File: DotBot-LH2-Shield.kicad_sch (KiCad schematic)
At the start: 15 parts, among them J1 Conn_01x04, J1 Conn_01x10, U1 LSM303AGR, U4 TS4231

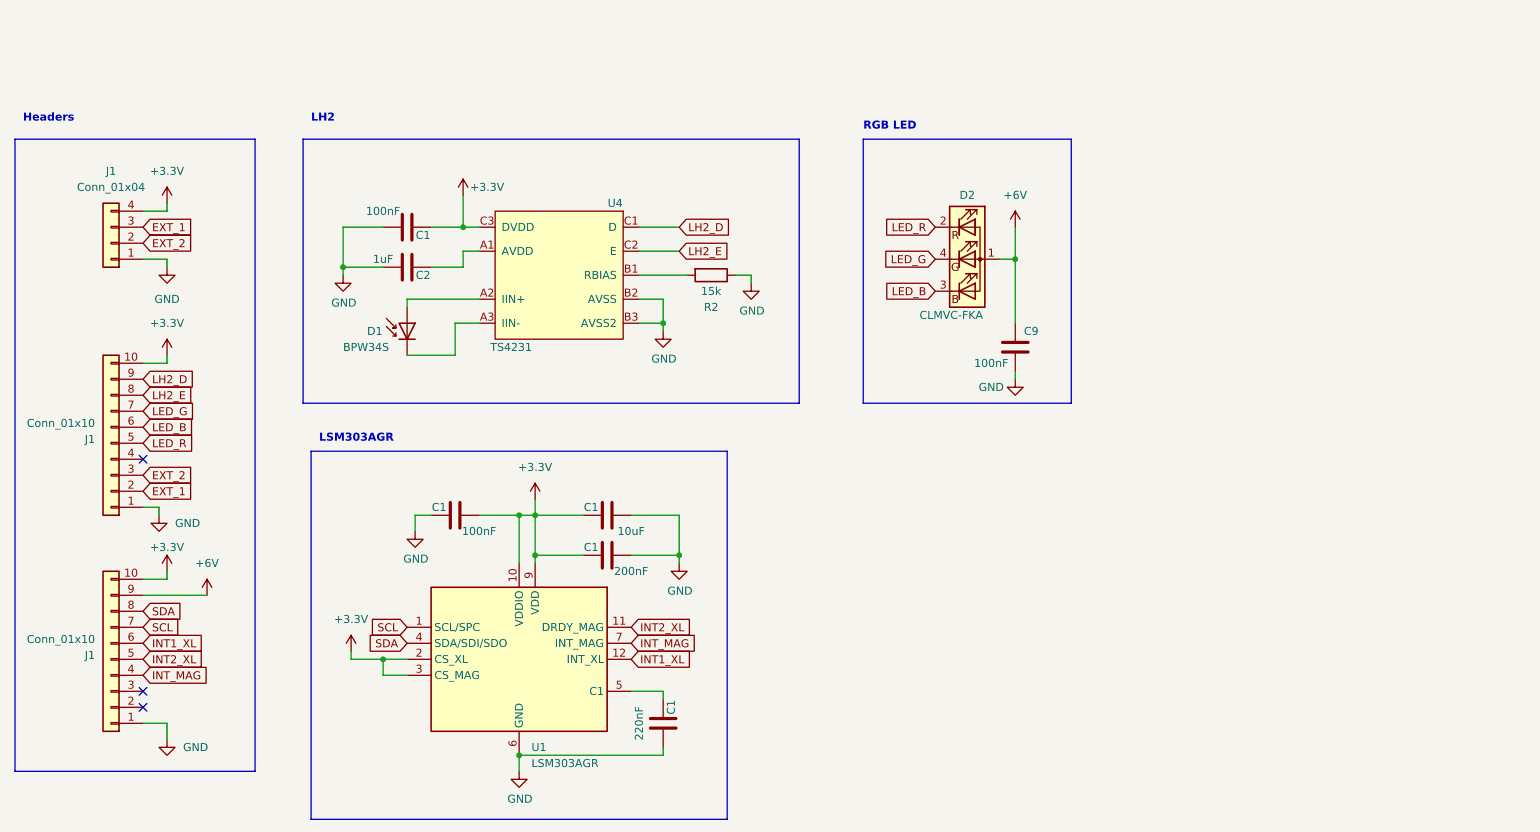
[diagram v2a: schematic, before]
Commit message: DotBot-LH2-Shield: rework IMU and RGB LED
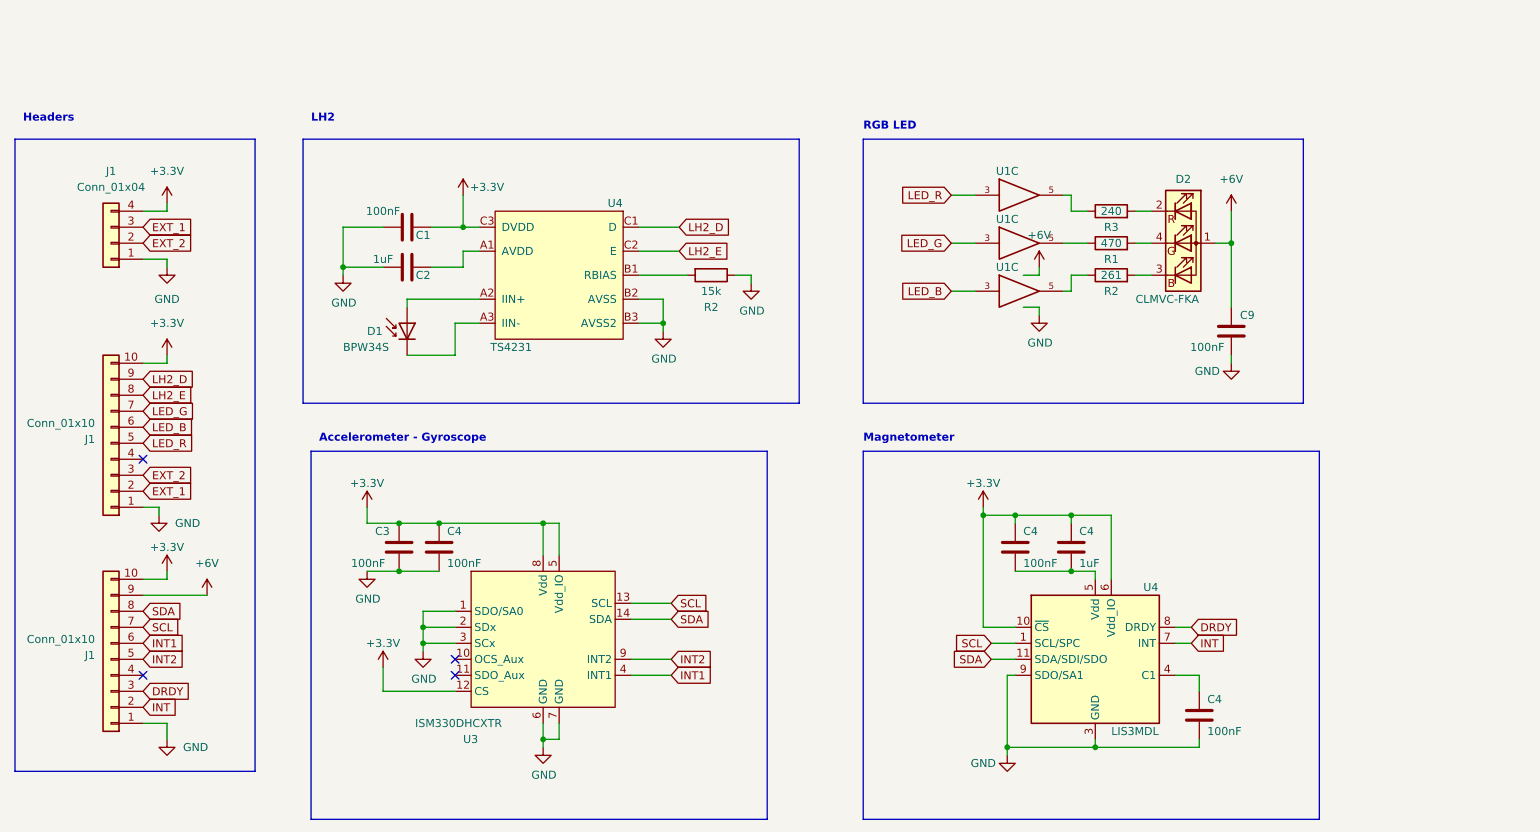
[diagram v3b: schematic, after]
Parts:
- removed C1: 200nF, Capacitor_SMD:C_0603_1608Metric, symbol Device:C
- removed C1: 220nF, Capacitor_SMD:C_0603_1608Metric, symbol Device:C
- removed C1: 100nF, Capacitor_SMD:C_0603_1608Metric, symbol Device:C
- removed C1: 10uF, Capacitor_SMD:C_0603_1608Metric, symbol Device:C
- removed U1: LSM303AGR, Package_LGA:LGA-12_2x2mm_P0.5mm, symbol Sensor_Motion:LSM303C
- added C3, C4 (x3): 100nF, Capacitor_SMD:C_0603_1608Metric, symbol Device:C
- added C4: 1uF, Capacitor_SMD:C_0603_1608Metric, symbol Device:C
- added R1: 470, Resistor_SMD:R_0603_1608Metric, symbol Device:R
- added R2: 261, Resistor_SMD:R_0603_1608Metric, symbol Device:R
- added R3: 240, Resistor_SMD:R_0603_1608Metric, symbol Device:R
- added U1 (x3): 74LVC3G34, DotBot:SOT833-1-8_1x1.95_Pitch0.5mm, symbol 74xGxx:74LVC3G34
- added U3: ISM330DHCXTR, Package_LGA:Bosch_LGA-14_3x2.5mm_P0.5mm, symbol DotBot:ISM330DHCXTR
- added U4: LIS3MDL, Package_LGA:LGA-12_2x2mm_P0.5mm, symbol Sensor_Magnetic:LIS3MDL
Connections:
- net +3V3: now also C3.1, C4.1, C4.1, C4.1, U3.12 (CS), U3.5 (Vdd_IO), U3.8 (Vdd), U4.10 (~{CS}), U4.6 (Vdd_IO)
- net +6V: now also U1.8 (VCC), U1.8 (VCC), U1.8 (VCC)
- net GND: now also C3.2, C4.2, C4.2, U1.4 (GND), U1.4 (GND), U1.4 (GND), U3.1 (SDO/SA0), U3.2 (SDx), U3.3 (SCx), U3.6 (GND), U3.7 (GND), U4.12 (GND), U4.2 (GND), U4.3 (GND), U4.9 (SDO/SA1)
- net LED_B: now also U1.3; no longer D2.3 (BK)
- net LED_G: now also U1.3; no longer D2.4 (GK)
- net LED_R: now also U1.3; no longer D2.2 (RK)
- net SCL: now also U3.13 (SCL), U4.1 (SCL/SPC)
- net SDA: now also U3.14 (SDA), U4.11 (SDA/SDI/SDO)
- net INT: now reaches J1.2 (Pin_2)
- net INT: now also U4.7 (INT)
- net DRDY: now reaches J1.3 (Pin_3)
- net DRDY: now also U4.8 (DRDY)
- net INT1_XL renamed INT1
- net INT1: now also U3.4 (INT1)
- net INT2_XL renamed INT2
- net INT2: now also U3.9 (INT2)
- net INT_MAG: no longer names the net of J1.4 (Pin_4)
- new net: C4.2, C4.2, U4.5 (Vdd)
- new net: D2.2 (RK), R3.2
- new net: D2.3 (BK), R2.2
- new net: D2.4 (GK), R1.2
- new net: R1.1, U1.5
- new net: R2.1, U1.5
- new net: C4.1, U4.4 (C1)
- new net: R3.1, U1.5
- no-connect marks 3 -> 4
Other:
- note added: "Accelerometer - Gyroscope"
- note added: "Magnetometer"
- note removed: "LSM303AGR"
- moved on the sheet: C9, D2

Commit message: DotBot-LH2-Shield: update BOM
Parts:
- C3, C4: Price $0.1 -> 0.1
- R1: Price $0.35 -> 0.35
- R2, R3: Price $0.19 -> 0.19
- U1: Price $0.46 -> 0.46
- U3: Price $11.34 -> 11.34
- U4: Link (none) -> https://www.digikey.fr/short/rzjc85mw; Manufacturer (none) -> STMicroelectronics; Mfr Part Number (none) -> 497-13892-1-ND; Price (none) -> 1.962
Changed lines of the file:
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@@
       (effects (font (size 1.27 1.27)) hide)
     )
-    (property "Price" "$0.1" (at 195.58 99.06 0)
+    (property "Price" "0.1" (at 195.58 99.06 0)
       (effects (font (size 1.27 1.27)) hide)
     )
@@
       (effects (font (size 1.27 1.27)) hide)
     )
-    (property "Datasheet" "~" (at 213.36 52.07 0)
+    (property "Datasheet" "https://media.digikey.com/pdf/Data%20Sheets/CREE%20Power/CLMVC-FKA_Rev13_2021.pdf" (at 213.36 52.07 0)
       (effects (font (size 1.27 1.27)) hide)
     )
@@
       (effects (font (size 1.27 1.27)) hide)
     )
-    (property "Price" "$0.1" (at 88.9 99.06 0)
+    (property "Price" "0.1" (at 88.9 99.06 0)
       (effects (font (size 1.27 1.27)) hide)
     )
@@
       (effects (font (size 1.27 1.27)) hide)
     )
-    (property "Price" "$0.46" (at 187.96 50.8 0)
+    (property "Price" "0.46" (at 187.96 50.8 0)
       (effects (font (size 1.27 1.27)) hide)
     )
@@
       (effects (font (size 1.27 1.27)) hide)
     )
-    (property "Price" "$0.46" (at 187.96 58.42 0)
+    (property "Price" "0.46" (at 187.96 58.42 0)
       (effects (font (size 1.27 1.27)) hide)
     )
@@
       (effects (font (size 1.27 1.27)) hide)
     )
-    (property "Price" "$0.1" (at 95.25 99.06 0)
+    (property "Price" "0.1" (at 95.25 99.06 0)
       (effects (font (size 1.27 1.27)) hide)
     )
@@
       (effects (font (size 1.27 1.27)) hide)
     )
-    (property "Price" "$0.1" (at 186.69 99.06 0)
+    (property "Price" "0.1" (at 186.69 99.06 0)
       (effects (font (size 1.27 1.27)) hide)
     )
@@
       (effects (font (size 1.27 1.27)) hide)
     )
-    (property "Price" "$0.19" (at 201.93 55.88 0)
+    (property "Price" "0.19" (at 201.93 55.88 0)
       (effects (font (size 1.27 1.27)) hide)
     )
@@
     )
     (property "Datasheet" "https://www.st.com/resource/en/datasheet/lis3mdl.pdf" (at 237.49 127 0)
+      (effects (font (size 1.27 1.27)) hide)
+    )
+    (property "Link" "https://www.digikey.fr/short/rzjc85mw" (at 199.39 116.84 0)
+      (effects (font (size 1.27 1.27)) hide)
+    )
+    (property "Manufacturer" "STMicroelectronics" (at 199.39 116.84 0)
+      (effects (font (size 1.27 1.27)) hide)
+    )
+    (property "Mfr Part Number" "497-13892-1-ND" (at 199.39 116.84 0)
+      (effects (font (size 1.27 1.27)) hide)
+    )
+    (property "Price" "1.962" (at 199.39 116.84 0)
       (effects (font (size 1.27 1.27)) hide)
     )
@@
       (effects (font (size 1.27 1.27)) hide)
     )
-    (property "Price" "$0.1" (at 215.9 125.73 0)
+    (property "Price" "0.1" (at 215.9 125.73 0)
       (effects (font (size 1.27 1.27)) hide)
     )
@@
       (effects (font (size 1.27 1.27)) hide)
     )
-    (property "Price" "$0.35" (at 201.93 50.8 0)
+    (property "Price" "0.35" (at 201.93 50.8 0)
       (effects (font (size 1.27 1.27)) hide)
     )
@@
       (effects (font (size 1.27 1.27)) hide)
     )
-    (property "Price" "$0.19" (at 201.93 45.72 0)
+    (property "Price" "0.19" (at 201.93 45.72 0)
       (effects (font (size 1.27 1.27)) hide)
     )
@@
       (effects (font (size 1.27 1.27)) hide)
     )
-    (property "Price" "$0.46" (at 187.96 43.18 0)
+    (property "Price" "0.46" (at 187.96 43.18 0)
       (effects (font (size 1.27 1.27)) hide)
     )
@@
       (effects (font (size 1.27 1.27)) hide)
     )
-    (property "Price" "$11.34" (at 110.49 113.03 0)
-      (effects (font (size 1.27 1.27)) hide)
-    )
+    (property "Price" "11.34" (at 110.49 113.03 0)
+      (effects (font (size 1.27 1.27)) hide)
+    )

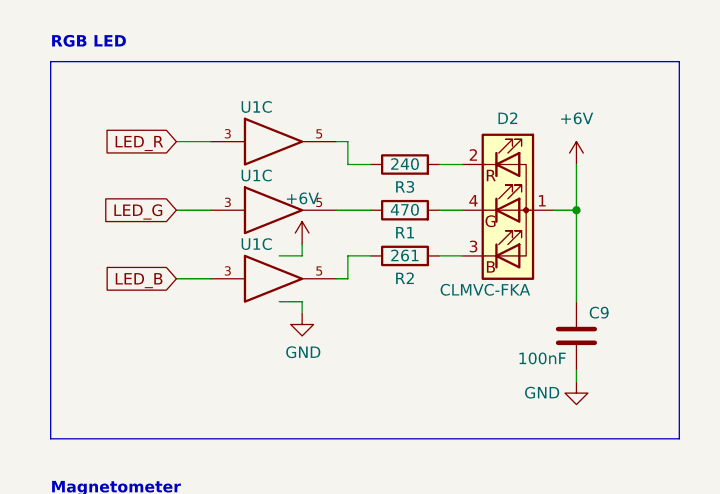
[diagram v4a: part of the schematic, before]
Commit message: Recalculate RGB resistors for 6v instead of 3.7v
the resistors for the RGB led were calculated for the minimote, which works with a  Li-ion 3.7v battery
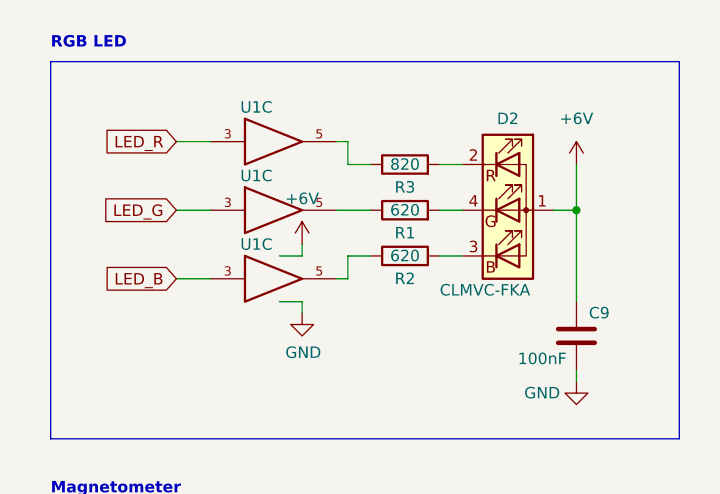
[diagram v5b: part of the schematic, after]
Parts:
- R1: value 470 -> 620
- R2: value 261 -> 620
- R3: value 240 -> 820
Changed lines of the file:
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@@
       (effects (font (size 1.27 1.27)))
     )
-    (property "Value" "261" (at 201.93 55.88 90)
+    (property "Value" "620" (at 201.93 55.88 90)
       (effects (font (size 1.27 1.27)))
     )
@@
       (effects (font (size 1.27 1.27)))
     )
-    (property "Value" "470" (at 201.93 50.8 90)
+    (property "Value" "620" (at 201.93 50.8 90)
       (effects (font (size 1.27 1.27)))
     )
@@
       (effects (font (size 1.27 1.27)))
     )
-    (property "Value" "240" (at 201.93 45.72 90)
-      (effects (font (size 1.27 1.27)))
-    )
+    (property "Value" "820" (at 201.93 45.72 90)
+      (effects (font (size 1.27 1.27)))
+    )

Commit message: DotBot-LH2-Shield: cleanup BOM
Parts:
- C1, C9: AISLER_MPN (none) -> CL10B104KB8NNWC; Manufacturer (none) -> Samsung Electro-Mechanics; Price 0.005 -> 0.004
- C2: AISLER_MPN (none) -> CL10A105KA8NNNC; Manufacturer (none) -> Samsung Electro-Mechanics; Mfr Part Number CL10A105KA8NNNC -> 1276-1102-1-ND; Price 0.0085 -> 0.007
- C3, C4: Price 0.1 -> 0.004
- C4: AISLER_MPN CL10B104KB8NNWC -> CL10A105KA8NNNC; Link https://www.digikey.fr/short/pm3hbfq0 -> https://www.digikey.fr/short/qjvrwt85; Mfr Part Number CL10B104KB8NNWC -> 1276-1102-1-ND; Price 0.1 -> 0.007
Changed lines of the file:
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@@
       (effects (font (size 1.27 1.27)) hide)
     )
-    (property "Datasheet" "http://www.samsungsem.com/kr/support/product-search/mlcc/CL10B104KB8NNWC.jsp" (at 195.58 99.06 0)
-      (effects (font (size 1.27 1.27)) hide)
-    )
-    (property "Link" "https://www.digikey.fr/short/pm3hbfq0" (at 195.58 99.06 0)
+    (property "Datasheet" "https://media.digikey.com/pdf/Data%20Sheets/Samsung%20PDFs/CL10A105KA8NNNC_Spec.pdf" (at 195.58 99.06 0)
+      (effects (font (size 1.27 1.27)) hide)
+    )
+    (property "Link" "https://www.digikey.fr/short/qjvrwt85" (at 195.58 99.06 0)
       (effects (font (size 1.27 1.27)) hide)
     )
@@
       (effects (font (size 1.27 1.27)) hide)
     )
-    (property "Mfr Part Number" "CL10B104KB8NNWC" (at 195.58 99.06 0)
-      (effects (font (size 1.27 1.27)) hide)
-    )
-    (property "Price" "0.1" (at 195.58 99.06 0)
-      (effects (font (size 1.27 1.27)) hide)
-    )
-    (property "AISLER_MPN" "CL10B104KB8NNWC" (at 195.58 99.06 0)
+    (property "Mfr Part Number" "1276-1102-1-ND " (at 195.58 99.06 0)
+      (effects (font (size 1.27 1.27)) hide)
+    )
+    (property "Price" "0.007" (at 195.58 99.06 0)
+      (effects (font (size 1.27 1.27)) hide)
+    )
+    (property "AISLER_MPN" "CL10A105KA8NNNC" (at 195.58 99.06 0)
       (effects (font (size 1.27 1.27)) hide)
     )
@@
       (effects (font (size 1.27 1.27)) hide)
     )
-    (property "Datasheet" "http://www.samsungsem.com/kr/support/product-search/mlcc/CL10B104KB8NNWC.jsp" (at 88.9 99.06 0)
+    (property "Datasheet" "https://media.digikey.com/pdf/Data%20Sheets/Samsung%20PDFs/CL10B104KB8NNWC_Spec.pdf" (at 88.9 99.06 0)
       (effects (font (size 1.27 1.27)) hide)
     )
@@
       (effects (font (size 1.27 1.27)) hide)
     )
-    (property "Price" "0.1" (at 88.9 99.06 0)
+    (property "Price" "0.004" (at 88.9 99.06 0)
       (effects (font (size 1.27 1.27)) hide)
     )
@@
       (effects (font (size 1.27 1.27)) hide)
     )
-    (property "Datasheet" "http://www.samsungsem.com/kr/support/product-search/mlcc/CL10B104KB8NNWC.jsp" (at 95.25 99.06 0)
+    (property "Datasheet" "https://media.digikey.com/pdf/Data%20Sheets/Samsung%20PDFs/CL10B104KB8NNWC_Spec.pdf" (at 95.25 99.06 0)
       (effects (font (size 1.27 1.27)) hide)
     )
@@
       (effects (font (size 1.27 1.27)) hide)
     )
-    (property "Price" "0.1" (at 95.25 99.06 0)
+    (property "Price" "0.004" (at 95.25 99.06 0)
       (effects (font (size 1.27 1.27)) hide)
     )
@@
       (effects (font (size 1.27 1.27)) hide)
     )
-    (property "Datasheet" "http://www.samsungsem.com/kr/support/product-search/mlcc/CL10B104KB8NNWC.jsp" (at 186.69 99.06 0)
+    (property "Datasheet" "https://media.digikey.com/pdf/Data%20Sheets/Samsung%20PDFs/CL10B104KB8NNWC_Spec.pdf" (at 186.69 99.06 0)
       (effects (font (size 1.27 1.27)) hide)
     )
@@
       (effects (font (size 1.27 1.27)) hide)
     )
-    (property "Price" "0.1" (at 186.69 99.06 0)
+    (property "Price" "0.004" (at 186.69 99.06 0)
       (effects (font (size 1.27 1.27)) hide)
     )
@@
       (effects (font (size 1.27 1.27)) hide)
     )
-    (property "Datasheet" "http://www.samsungsem.com/kr/support/product-search/mlcc/CL10B104KB8NNWC.jsp" (at 220.98 64.77 0)
+    (property "Datasheet" "https://media.digikey.com/pdf/Data%20Sheets/Samsung%20PDFs/CL10B104KB8NNWC_Spec.pdf" (at 220.98 64.77 0)
       (effects (font (size 1.27 1.27)) hide)
     )
@@
       (effects (font (size 1.27 1.27)) hide)
     )
-    (property "Price" "0.005" (at 220.98 64.77 0)
+    (property "Price" "0.004" (at 220.98 64.77 0)
+      (effects (font (size 1.27 1.27)) hide)
+    )
+    (property "AISLER_MPN" "CL10B104KB8NNWC" (at 220.98 64.77 0)
+      (effects (font (size 1.27 1.27)) hide)
+    )
+    (property "Manufacturer" "Samsung Electro-Mechanics" (at 220.98 64.77 0)
       (effects (font (size 1.27 1.27)) hide)
     )
@@
       (effects (font (size 1.27 1.27)) hide)
     )
-    (property "Mfr Part Number" "CL10A105KA8NNNC" (at 90.17 54.61 0)
-      (effects (font (size 1.27 1.27)) hide)
-    )
-    (property "Price" "0.0085" (at 90.17 54.61 0)
+    (property "Mfr Part Number" "1276-1102-1-ND " (at 90.17 54.61 0)
+      (effects (font (size 1.27 1.27)) hide)
+    )
+    (property "Price" "0.007" (at 90.17 54.61 0)
+      (effects (font (size 1.27 1.27)) hide)
+    )
+    (property "AISLER_MPN" "CL10A105KA8NNNC" (at 90.17 54.61 0)
+      (effects (font (size 1.27 1.27)) hide)
+    )
+    (property "Manufacturer" "Samsung Electro-Mechanics" (at 90.17 54.61 0)
       (effects (font (size 1.27 1.27)) hide)
     )
@@
       (effects (font (size 1.27 1.27)) hide)
     )
-    (property "Datasheet" "http://www.samsungsem.com/kr/support/product-search/mlcc/CL10B104KB8NNWC.jsp" (at 215.9 125.73 0)
+    (property "Datasheet" "https://media.digikey.com/pdf/Data%20Sheets/Samsung%20PDFs/CL10B104KB8NNWC_Spec.pdf" (at 215.9 125.73 0)
       (effects (font (size 1.27 1.27)) hide)
     )
@@
       (effects (font (size 1.27 1.27)) hide)
     )
-    (property "Price" "0.1" (at 215.9 125.73 0)
+    (property "Price" "0.004" (at 215.9 125.73 0)
       (effects (font (size 1.27 1.27)) hide)
     )
@@
       (effects (font (size 1.27 1.27)) hide)
     )
-    (property "Datasheet" "http://www.samsungsem.com/kr/support/product-search/mlcc/CL10B104KB8NNWC.jsp" (at 90.17 48.26 0)
+    (property "Datasheet" "https://media.digikey.com/pdf/Data%20Sheets/Samsung%20PDFs/CL10B104KB8NNWC_Spec.pdf" (at 90.17 48.26 0)
       (effects (font (size 1.27 1.27)) hide)
     )
@@
       (effects (font (size 1.27 1.27)) hide)
     )
-    (property "Price" "0.005" (at 90.17 48.26 0)
-      (effects (font (size 1.27 1.27)) hide)
-    )
+    (property "Price" "0.004" (at 90.17 48.26 0)
+      (effects (font (size 1.27 1.27)) hide)
+    )
+    (property "AISLER_MPN" "CL10B104KB8NNWC" (at 90.17 48.26 0)
+      (effects (font (size 1.27 1.27)) hide)
+    )
+    (property "Manufacturer" "Samsung Electro-Mechanics" (at 90.17 48.26 0)
+      (effects (font (size 1.27 1.27)) hide)
+    )

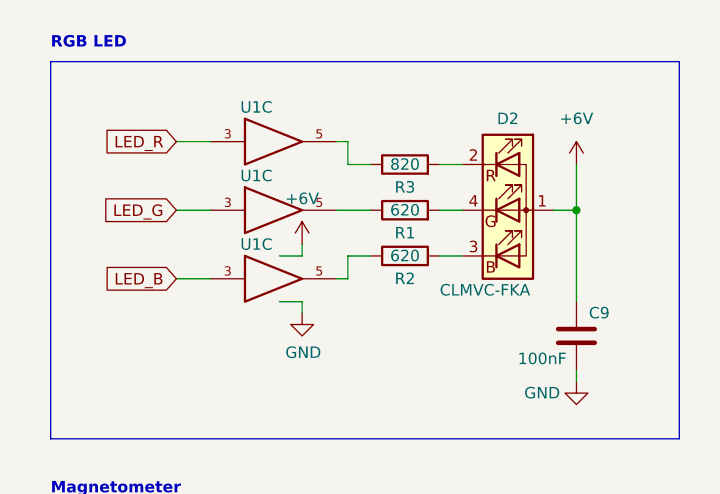
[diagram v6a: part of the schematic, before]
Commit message: DotBot-LH2-Shield: improve routing and power planes
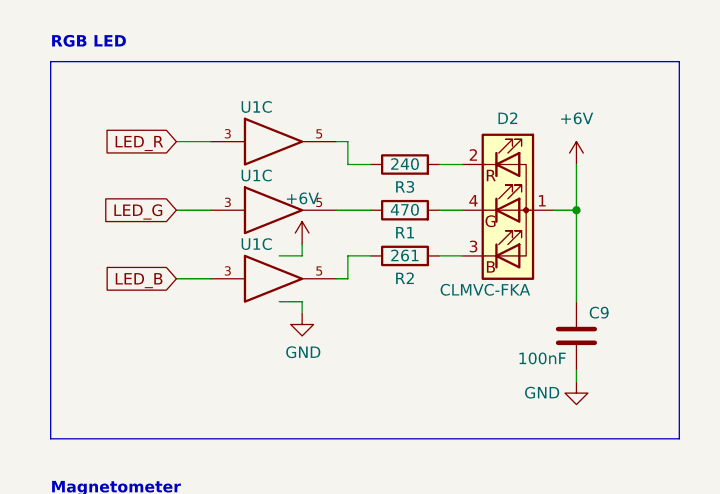
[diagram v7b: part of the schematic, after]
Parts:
- R1: value 620 -> 470
- R2: value 620 -> 261
- R3: value 820 -> 240
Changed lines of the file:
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@@
       (effects (font (size 1.27 1.27)))
     )
-    (property "Value" "620" (at 201.93 55.88 90)
+    (property "Value" "261" (at 201.93 55.88 90)
       (effects (font (size 1.27 1.27)))
     )
@@
       (effects (font (size 1.27 1.27)))
     )
-    (property "Value" "620" (at 201.93 50.8 90)
+    (property "Value" "470" (at 201.93 50.8 90)
       (effects (font (size 1.27 1.27)))
     )
@@
       (effects (font (size 1.27 1.27)))
     )
-    (property "Value" "820" (at 201.93 45.72 90)
-      (effects (font (size 1.27 1.27)))
-    )
+    (property "Value" "240" (at 201.93 45.72 90)
+      (effects (font (size 1.27 1.27)))
+    )
